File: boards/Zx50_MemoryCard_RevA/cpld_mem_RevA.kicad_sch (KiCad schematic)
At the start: 33 parts, among them J2 JTAG, U10 CY7C1049GN, U11 CY7C1049GN, U12 SST39SF040, U8 ATF1508AS-10AU100, U9 IS61C256AL-12JLI

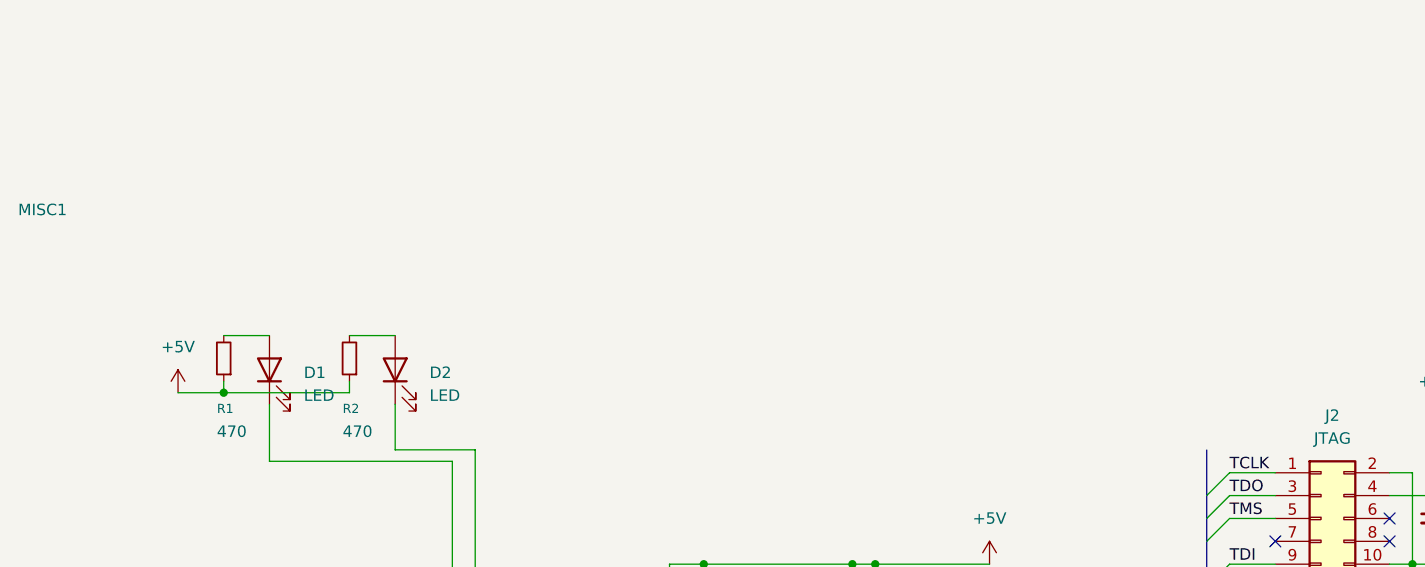
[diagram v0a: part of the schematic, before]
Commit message: rewrite cpld code in more structured Amaranth state machine.
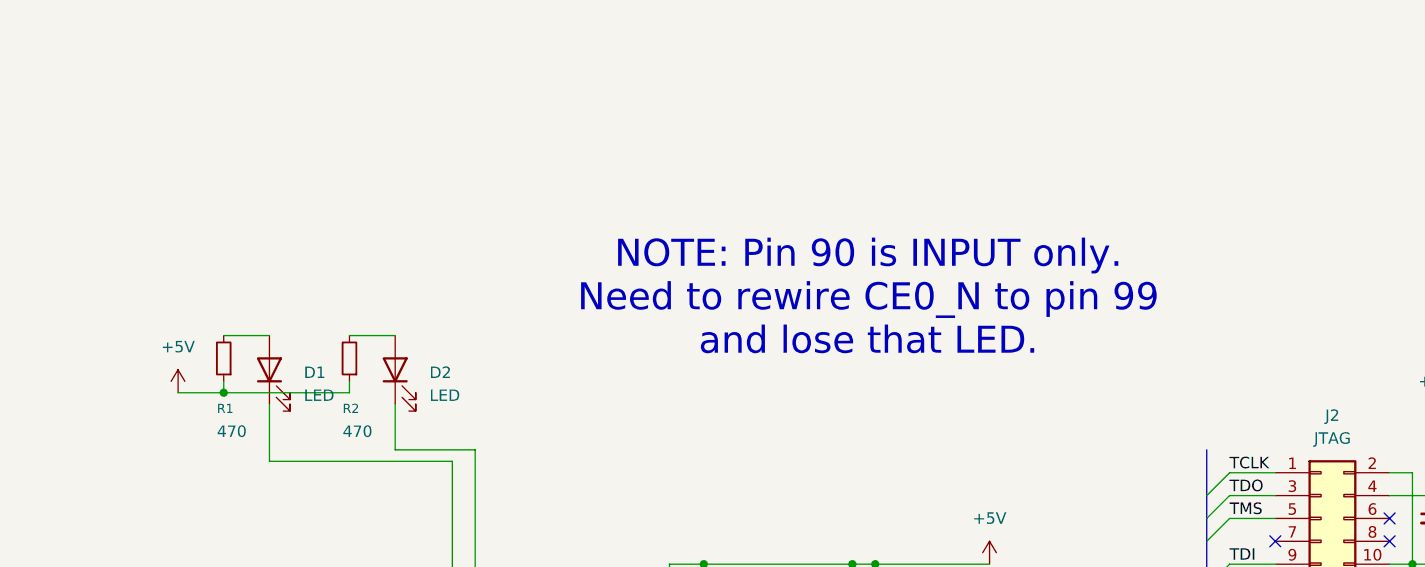
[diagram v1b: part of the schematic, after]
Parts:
- removed MISC1: ~, DIP-32 socket, symbol zx50_symbols:DIP-32_Socket
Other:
- note added: "NOTE: Pin 90 is INPUT only. Need to rewire CE0_N to pin 99 and lose that LED."
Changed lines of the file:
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@@
 		(members "L_A[0..10]" "~CE0~" "~CE1~" "~OE~" "~WE~" "~CE2~")
 	)
+	(text "NOTE: Pin 90 is INPUT only.\nNeed to rewire CE0_N to pin 99 \nand lose that LED."
+		(exclude_from_sim no)
+		(at 121.158 68.326 0)
+		(effects
+			(font
+				(size 3 3)
+			)
+		)
+	)
 	(junction
 		(at 102.87 97.79)
@@
 					(unit 1)
 				)
-			)
-		)
-	)
-	(symbol
-		(lib_id "zx50_symbols:DIP-32_Socket")
-		(at 25.4 59.69 0)
-		(unit 1)
-		(exclude_from_sim no)
-		(in_bom no)
-		(on_board no)
-		(dnp no)
-		(fields_autoplaced yes)
-		(property "Reference" "MISC1"
-			(at 26.67 58.4199 0)
-			(effects
-				(font
-					(size 1.27 1.27)
-				)
-				(justify left)
-			)
-		)
-		(property "Value" "~"
-			(at 26.67 60.9599 0)
-			(effects
-				(font
-					(size 1.27 1.27)
-				)
-				(justify left)
-			)
-		)
-		(property "Footprint" "DIP-32 socket"
-			(at 25.4 59.69 0)
-			(effects
-				(font
-					(size 1.27 1.27)
-				)
-				(hide yes)
-			)
-		)
-		(property "Datasheet" ""
-			(at 25.4 59.69 0)
-			(effects
-				(font
-					(size 1.27 1.27)
-				)
-				(hide yes)
-			)
-		)
-		(property "Description" ""
-			(at 25.4 59.69 0)
-			(effects
-				(font
-					(size 1.27 1.27)
-				)
-				(hide yes)
-			)
-		)
-		(property "DigiKey_PN" "123-AR32-HZL/01-TT-ND"
-			(at 25.4 59.69 0)
-			(effects
-				(font
-					(size 1.27 1.27)
-				)
-				(hide yes)
-			)
-		)
-		(property "SKU" ""
-			(at 25.4 59.69 0)
-			(effects
-				(font
-					(size 1.27 1.27)
-				)
-				(hide yes)
-			)
-		)
-		(instances
-			(project ""
-				(path "/024a2433-248f-41c0-8a0c-ac9ea528ccd5/77747e00-68ea-483a-b865-379235adbc78"
-					(reference "MISC1")
-					(unit 1)
-				)
